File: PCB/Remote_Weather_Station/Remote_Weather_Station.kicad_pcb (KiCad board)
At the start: 4 copper layers, 0 parts

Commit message: Add files via upload
Laid out PDN
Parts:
- added C101: 1u, Capacitor_SMD:C_0805_2012Metric, F.Cu at (176.0, 92.3)
- added C102: 1u, Capacitor_SMD:C_0805_2012Metric, F.Cu at (176.0, 95.3)
- added C103: 100n, Capacitor_SMD:C_0805_2012Metric, F.Cu at (176.0, 98.3)
- added C104: 1u, Capacitor_SMD:C_0805_2012Metric, F.Cu at (176.0, 101.3)
- added C105: 1u, Capacitor_SMD:C_0805_2012Metric, F.Cu at (176.0, 104.4)
- added C106: 1u, Capacitor_SMD:C_0805_2012Metric, F.Cu at (176.0, 107.4)
- added C107: 1u, Capacitor_SMD:C_0805_2012Metric, F.Cu at (180.5, 92.3)
- added C108: 1u, Capacitor_SMD:C_0805_2012Metric, F.Cu at (180.5, 95.3)
- added C109: 1u, Capacitor_SMD:C_0805_2012Metric, F.Cu at (180.5, 98.3)
- added C110: 1u, Capacitor_SMD:C_0805_2012Metric, F.Cu at (180.5, 101.3)
- added C111: 1u, Capacitor_SMD:C_0805_2012Metric, F.Cu at (180.5, 104.4)
- added C112: 1u, Capacitor_SMD:C_0805_2012Metric, F.Cu at (180.5, 107.4)
- added C113: 1u, Capacitor_SMD:C_0805_2012Metric, F.Cu at (184.9, 92.3)
- added C114: 1u, Capacitor_SMD:C_0805_2012Metric, F.Cu at (184.9, 95.3)
- added C115: 1u, Capacitor_SMD:C_0805_2012Metric, F.Cu at (184.9, 98.3)
- added C116: 1u, Capacitor_SMD:C_0805_2012Metric, F.Cu at (184.9, 101.3)
- added C117: 1u, Capacitor_SMD:C_0805_2012Metric, F.Cu at (184.9, 104.4)
- added C201: 100n, Capacitor_SMD:C_0805_2012Metric, F.Cu at (47.4, 98.2)
- added C202: 10u, Capacitor_SMD:C_0805_2012Metric, F.Cu at (39.6, 102.5)
- added C203: 10u, Capacitor_SMD:C_0805_2012Metric, F.Cu at (39.6, 100.4)
- added C204: 47u, Capacitor_SMD:C_1206_3216Metric, F.Cu at (56.5, 99.6)
- added C205: 10u, Capacitor_SMD:C_0805_2012Metric, F.Cu at (60.5, 104.5)
- added C206: 22u, Capacitor_SMD:C_1206_3216Metric, F.Cu at (71.7, 101.1)
- added C207: 10u, Capacitor_SMD:C_0805_2012Metric, F.Cu at (60.6, 116.8)
- added C208: 22u, Capacitor_SMD:C_1206_3216Metric, F.Cu at (71.6, 113.9)
- added C209: 100n, Capacitor_SMD:C_0805_2012Metric, F.Cu at (47.5, 110.9)
- added C210: 10u, Capacitor_SMD:C_0805_2012Metric, F.Cu at (39.9, 113.1)
- added C211: 10u, Capacitor_SMD:C_0805_2012Metric, F.Cu at (39.9, 115.1)
- added C212: 47u, Capacitor_SMD:C_1206_3216Metric, F.Cu at (56.7, 112.3)
- added D101: RED_LED, LED_SMD:LED_0603_1608Metric, F.Cu at (188.9, 125.5)
- added H101: MountingHole, MountingHole:MountingHole_2.7mm_M2.5, F.Cu at (151.5, 56.6)
- added H102: MountingHole, MountingHole:MountingHole_2.7mm_M2.5, F.Cu at (151.5, 63.5)
- added H103: MountingHole, MountingHole:MountingHole_2.7mm_M2.5, F.Cu at (151.5, 70.5)
- added H104: MountingHole, MountingHole:MountingHole_2.7mm_M2.5, F.Cu at (151.5, 77.4)
- added J101: UART, Connector_PinHeader_2.54mm:PinHeader_1x06_P2.54mm_Vertical, F.Cu at (184.5, 111.2)
- added J102: Stemma_QT_Connector, Connector_JST:JST_SH_BM04B-SRSS-TB_1x04-1MP_P1.00mm_Vertical, F.Cu at (191.3, 121.1)
- added J103: wire_bus, Terminal_Blocks:WJ250B-3.5-12P-11-00A, F.Cu at (164.9, 164.5)
- added J105: power_in, Terminal_Blocks:DBT50G-7.62-4P-BK-P, F.Cu at (106.5, 101.5)
- added L201: 4.7u, Inductor_SMD:L_Vishay_IFSC-1515AH_4x4x1.8mm, F.Cu at (51.4, 99.5)
- added L202: 4.7u, Inductor_SMD:L_Vishay_IFSC-1515AH_4x4x1.8mm, F.Cu at (51.7, 112.2)
- added R101: 680, Resistor_SMD:R_0603_1608Metric_Pad0.98x0.95mm_HandSolder, F.Cu at (162.9, 92.1)
- added R102: 4.7k, Resistor_SMD:R_0603_1608Metric_Pad0.98x0.95mm_HandSolder, F.Cu at (162.9, 94.6)
- added R103: 20, Resistor_SMD:R_0603_1608Metric_Pad0.98x0.95mm_HandSolder, F.Cu at (162.9, 97.1)
- added R104: 330, Resistor_SMD:R_0603_1608Metric_Pad0.98x0.95mm_HandSolder, F.Cu at (162.9, 99.6)
- added R105: 4.7k, Resistor_SMD:R_0603_1608Metric_Pad0.98x0.95mm_HandSolder, F.Cu at (162.9, 102.1)
- added R106: 4.7k, Resistor_SMD:R_0603_1608Metric_Pad0.98x0.95mm_HandSolder, F.Cu at (162.9, 104.6)
- added R107: 20, Resistor_SMD:R_0603_1608Metric_Pad0.98x0.95mm_HandSolder, F.Cu at (162.9, 107.1)
- added R108: 330, Resistor_SMD:R_0603_1608Metric_Pad0.98x0.95mm_HandSolder, F.Cu at (162.9, 109.6)
- added R109: 4.7k, Resistor_SMD:R_0603_1608Metric_Pad0.98x0.95mm_HandSolder, F.Cu at (167.3, 92.1)
- added R110: 820, Resistor_SMD:R_0603_1608Metric_Pad0.98x0.95mm_HandSolder, F.Cu at (167.3, 94.6)
- added R111: 15k, Resistor_SMD:R_0603_1608Metric_Pad0.98x0.95mm_HandSolder, F.Cu at (167.3, 97.1)
- added R112: 15k, Resistor_SMD:R_0603_1608Metric_Pad0.98x0.95mm_HandSolder, F.Cu at (167.3, 99.6)
- added R113: 10k, Resistor_SMD:R_0603_1608Metric_Pad0.98x0.95mm_HandSolder, F.Cu at (167.3, 102.1)
- added R114: 1k, Resistor_SMD:R_0603_1608Metric_Pad0.98x0.95mm_HandSolder, F.Cu at (167.3, 104.6)
- added R115: 10k, Resistor_SMD:R_0603_1608Metric_Pad0.98x0.95mm_HandSolder, F.Cu at (167.3, 107.1)
- added R116: 1k, Resistor_SMD:R_0603_1608Metric_Pad0.98x0.95mm_HandSolder, F.Cu at (167.3, 109.6)
- added R117: 10k, Resistor_SMD:R_0603_1608Metric_Pad0.98x0.95mm_HandSolder, F.Cu at (171.6, 92.1)
- added R118: 4.7k, Resistor_SMD:R_0603_1608Metric_Pad0.98x0.95mm_HandSolder, F.Cu at (171.6, 94.6)
- added R119: 4.7k, Resistor_SMD:R_0603_1608Metric_Pad0.98x0.95mm_HandSolder, F.Cu at (171.6, 97.1)
- added R120: 4.7k, Resistor_SMD:R_0603_1608Metric_Pad0.98x0.95mm_HandSolder, F.Cu at (171.6, 99.6)
- added R121: 1k, Resistor_SMD:R_0603_1608Metric_Pad0.98x0.95mm_HandSolder, F.Cu at (171.6, 102.1)
- added R201: 49.9k, Resistor_SMD:R_0603_1608Metric_Pad0.98x0.95mm_HandSolder, F.Cu at (54.5, 98.9)
- added R202: 10k, Resistor_SMD:R_0603_1608Metric_Pad0.98x0.95mm_HandSolder, F.Cu at (54.5, 102.2)
- added R203: 0, Resistor_SMD:R_0603_1608Metric_Pad0.98x0.95mm_HandSolder, F.Cu at (71.7, 105.1)
- added R204: 0, Resistor_SMD:R_0603_1608Metric_Pad0.98x0.95mm_HandSolder, F.Cu at (71.6, 117.9)
- added R205: 68k, Resistor_SMD:R_0603_1608Metric_Pad0.98x0.95mm_HandSolder, F.Cu at (54.8, 111.6)
- added R206: 10k, Resistor_SMD:R_0603_1608Metric_Pad0.98x0.95mm_HandSolder, F.Cu at (54.8, 118.2)
- added R207: 3.6k, Resistor_SMD:R_0603_1608Metric_Pad0.98x0.95mm_HandSolder, F.Cu at (54.8, 114.9)
- added SW101: SW_Push, Button_Switch_SMD:SW_SPST_TS-1088-xR020, F.Cu at (190.4, 111.2)
- added SW102: SW_Push, Button_Switch_SMD:SW_SPST_TS-1088-xR020, F.Cu at (190.4, 115.7)
- added U101: ESP32-WROOM-32D, RF_Module:ESP32-WROOM-32D, F.Cu at (131.6, 76.1)
- added U102: AD8227, Package_SO:SOIC-8_3.9x4.9mm_P1.27mm, F.Cu at (178.0, 112.2)
- added U103: AD8227, Package_SO:SOIC-8_3.9x4.9mm_P1.27mm, F.Cu at (178.0, 118.8)
- added U104: AD8227, Package_SO:SOIC-8_3.9x4.9mm_P1.27mm, F.Cu at (178.0, 125.4)
- added U105: SIM7600X, Modem_Footprint:SIM7600X, F.Cu at (137.3, 111.0)
- added U201: TPS561208DDCR, Package_TO_SOT_SMD:SOT-23-6, F.Cu at (43.5, 99.0)
- added U202: AMS1117-3.3, Package_TO_SOT_SMD:SOT-223-3_TabPin2, F.Cu at (66.0, 101.0)
- added U203: AMS1117-5.0, Package_TO_SOT_SMD:SOT-223-3_TabPin2, F.Cu at (66.0, 113.6)
- added U204: TPS561201DDCR, Package_TO_SOT_SMD:SOT-23-6, F.Cu at (43.7, 111.4)

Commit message: Add files via upload
PDN PCB v.1
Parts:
- moved C208 5.88 mm to (77.4, 114.8)
- moved R204 5.88 mm to (77.4, 118.9)
- moved U202 5.86 mm to (71.8, 100.7)
- moved U203 5.81 mm to (71.8, 113.3)
- moved R203 5.81 mm to (77.4, 106.2)
- moved C206 5.81 mm to (77.4, 102.2)
- moved C205 5.12 mm to (64.5, 101.2)
- moved C212 5.11 mm to (61.8, 112.0)
- moved C204 5.10 mm to (61.6, 99.5)
- moved C207 5.00 mm to (64.5, 113.7)
- moved R201 4.30 mm to (58.8, 98.9)
- moved R202 4.30 mm to (58.8, 102.2)
- moved R205 4.00 mm to (58.8, 111.5)
- moved R206 4.00 mm to (58.8, 118.1)
- moved R207 4.00 mm to (58.8, 114.8)
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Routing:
- net +12V: track 0.00 -> 21.2 mm
- net /PDN/6.3V_OUT: track 0.00 -> 18.7 mm
- net /PDN/4.6V_OUT: track 0.00 -> 18.6 mm
- net Net-(U204-VFB): track 0.00 -> 17.2 mm, vias 0 -> 2
- net Net-(U201-VFB): track 0.00 -> 15.9 mm, vias 0 -> 2
- net Net-(U201-SW): track 0.00 -> 11.2 mm, vias 0 -> 2
- net Net-(U204-SW): track 0.00 -> 11.0 mm, vias 0 -> 2
- net +5V: track 0.00 -> 8.70 mm, vias 0 -> 2
- net +3.3V: track 0.00 -> 8.70 mm, vias 0 -> 2
- net Net-(U201-VBST): track 0.00 -> 2.80 mm
- net Net-(U204-VBST): track 0.00 -> 2.69 mm
- net Net-(C208-Pad2): track 0.00 -> 1.65 mm
- net Net-(C206-Pad2): track 0.00 -> 1.65 mm
- net Net-(R205-Pad2): track 0.00 -> 1.50 mm
- net GND: vias 0 -> 16

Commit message: Add files via upload
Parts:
- added C106: 1u, Capacitor_SMD:C_0805_2012Metric, F.Cu at (89.7, 139.2)
- added C107: 1u, Capacitor_SMD:C_0805_2012Metric, F.Cu at (89.7, 142.2)
- added C120: 1u, Capacitor_SMD:C_0805_2012Metric, F.Cu at (89.7, 145.2)
- added C121: 1u, Capacitor_SMD:C_0805_2012Metric, F.Cu at (89.7, 148.2)
- added R102: 11k, Resistor_SMD:R_0603_1608Metric_Pad0.98x0.95mm_HandSolder, F.Cu at (94.1, 139.0)
- added R103: 11k, Resistor_SMD:R_0603_1608Metric_Pad0.98x0.95mm_HandSolder, F.Cu at (94.1, 141.5)
- added R124: 11k, Resistor_SMD:R_0603_1608Metric_Pad0.98x0.95mm_HandSolder, F.Cu at (94.1, 144.0)
- added R125: 11k, Resistor_SMD:R_0603_1608Metric_Pad0.98x0.95mm_HandSolder, F.Cu at (94.1, 146.5)
- renumbered C103 to C102, C104 to C103, C102 to C104, C106 to C108, C107 to C109, C108 to C110, C109 to C111, C110 to C112, C111 to C113, C112 to C114, C113 to C115, C117 to C116, C114 to C117, C115 to C118, C116 to C119, R102 to R104, R103 to R105, R104 to R106, R105 to R107, R106 to R108, R107 to R109, R108 to R110, R109 to R111, R110 to R112, R111 to R113, R112 to R114, R113 to R115, R114 to R116, R115 to R117, R116 to R118, R117 to R119, R121 to R120, R118 to R121, R119 to R122, R120 to R123, R207 to R206, R206 to R207, U105 to U102, U102 to U103, U103 to U104, U104 to U105
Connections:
- J102 pad MP: (no net) -> GND
- J103 pad 10: Green_Wire -> Green_Wire_in
- J103 pad 11: White_Wire -> White_Wire_in
- J103 pad 2: North_South_Ref -> /N_red_wire
- J103 pad 4: East_West_Ref -> /E_red_wire
- J103 pad 5: North_South_Ref -> /N_red_wire
- J103 pad 7: East_West_Ref -> /E_red_wire
- U103 pad 1: Green_Wire -> White_Wire
- U103 pad 4: White_Wire -> Green_Wire

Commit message: Add files via upload
PCB Progress, Layout coming along
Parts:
- R102, R103: value 11k -> 10k
- R112: renamed from R124; value 11k -> 10k
- R113: renamed from R125; value 11k -> 10k
- moved C101 133.1 mm to (43.0, 93.2)
- moved C104 133.1 mm to (43.0, 96.2)
- moved C105 133.1 mm to (43.0, 105.3)
- moved C109 133.1 mm to (47.4, 93.2)
- moved C110 133.1 mm to (47.4, 96.2)
- moved C111 133.1 mm to (47.4, 99.2)
- moved C115 133.1 mm to (47.4, 105.3)
- moved C116 133.1 mm to (47.4, 108.3)
- moved C117 133.1 mm to (51.9, 93.2)
- moved C118 133.1 mm to (51.9, 105.3)
- moved C119 133.1 mm to (51.9, 96.2)
- moved C120 133.1 mm to (51.9, 99.2)
- moved C121 133.1 mm to (51.9, 102.2)
- moved D101 133.1 mm to (55.8, 126.4)
- moved R101 133.1 mm to (29.9, 93.0)
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- renumbered C120 to C113, C121 to C114, C113 to C115, C114 to C116, C115 to C117, C116 to C118, C117 to C119, C118 to C120, C119 to C121, R112 to R114, R113 to R115, R114 to R116, R115 to R117, R116 to R118, R117 to R119, R118 to R120, R119 to R121, R120 to R122, R121 to R123, R122 to R124, R123 to R125
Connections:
- U101 pad 11: unconnected-(U101-IO26-Pad11) -> modem_tx
- U101 pad 12: unconnected-(U101-IO27-Pad12) -> modem_rx
- U102 pad 21: unconnected-(U102-RXD-Pad21) -> modem_rx
- U102 pad 22: unconnected-(U102-TXD-Pad22) -> modem_tx
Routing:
- net modem_rx: track 0.00 -> 42.9 mm
- net Flash: track 0.00 -> 42.3 mm, vias 0 -> 1
- net modem_tx: track 0.00 -> 39.4 mm
- net TX: track 0.00 -> 36.9 mm, vias 0 -> 1
- net RX: track 0.00 -> 33.7 mm, vias 0 -> 1
- net Reset: track 0.00 -> 21.1 mm
- net +3.3V: track 8.70 -> 16.0 mm
- net GND: vias 16 -> 24
- added copper zone on In2.Cu, net +12V

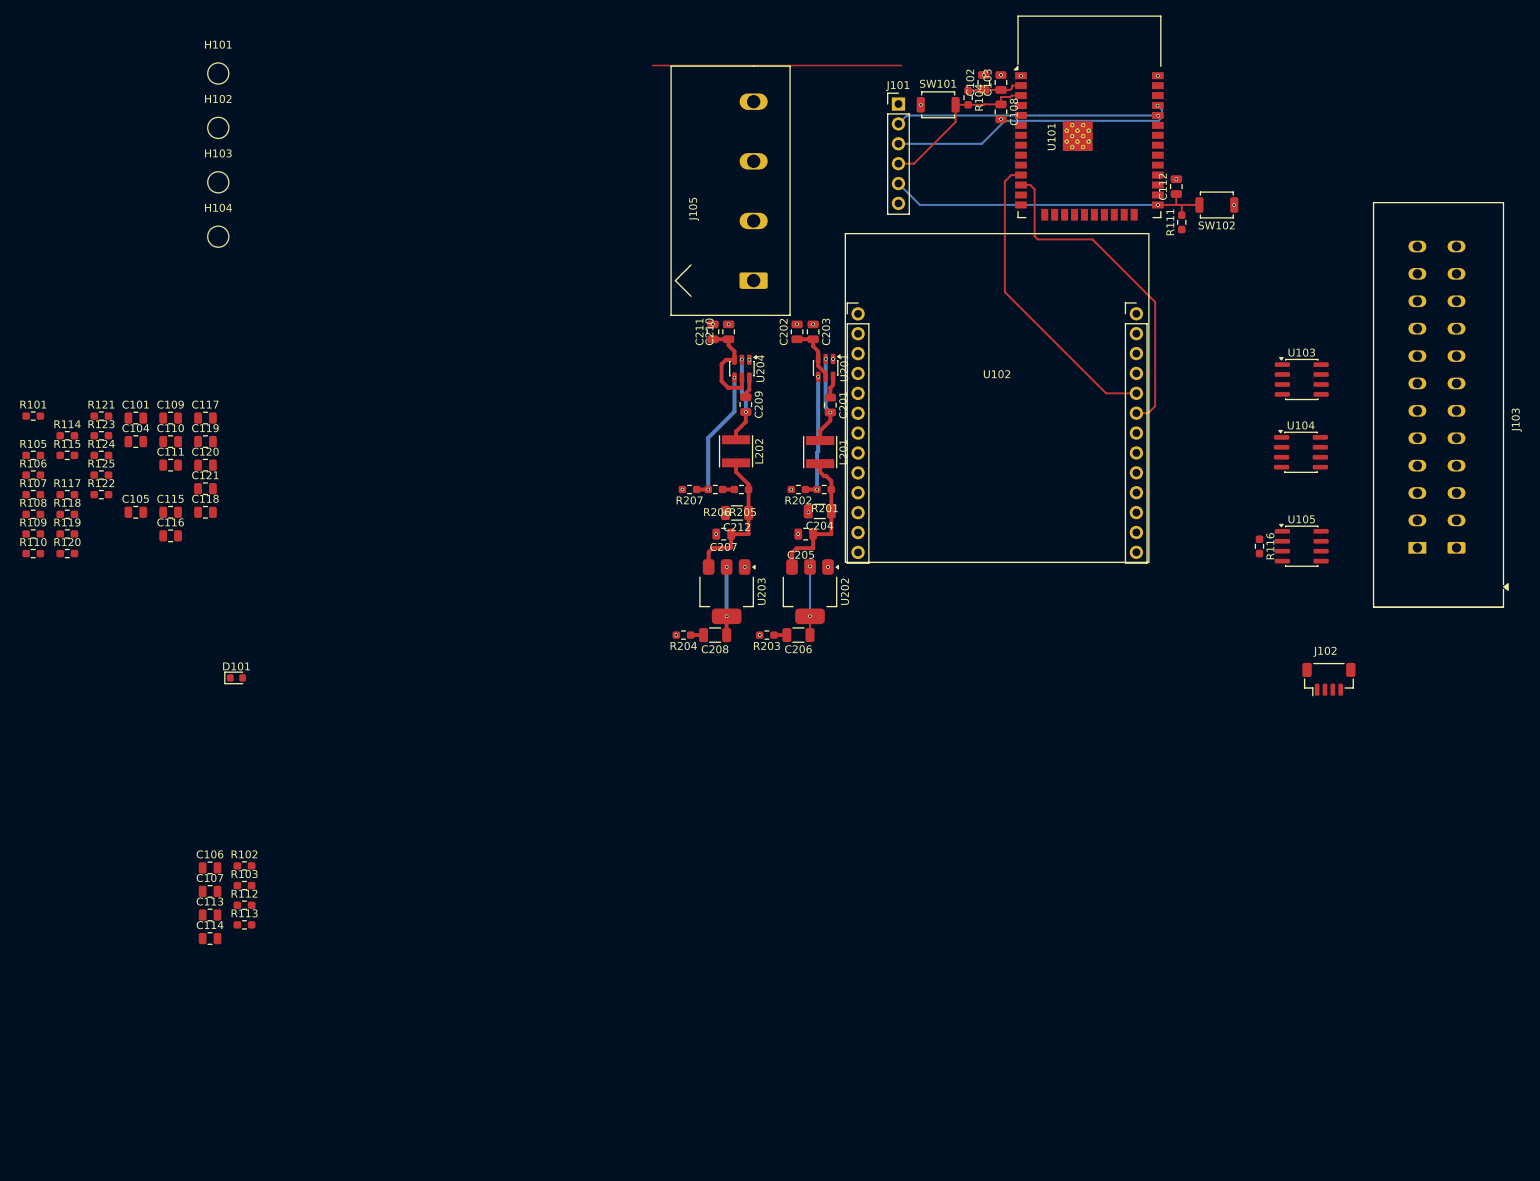
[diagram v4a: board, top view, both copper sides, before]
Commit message: Vias
Vias should be added and tied to pads
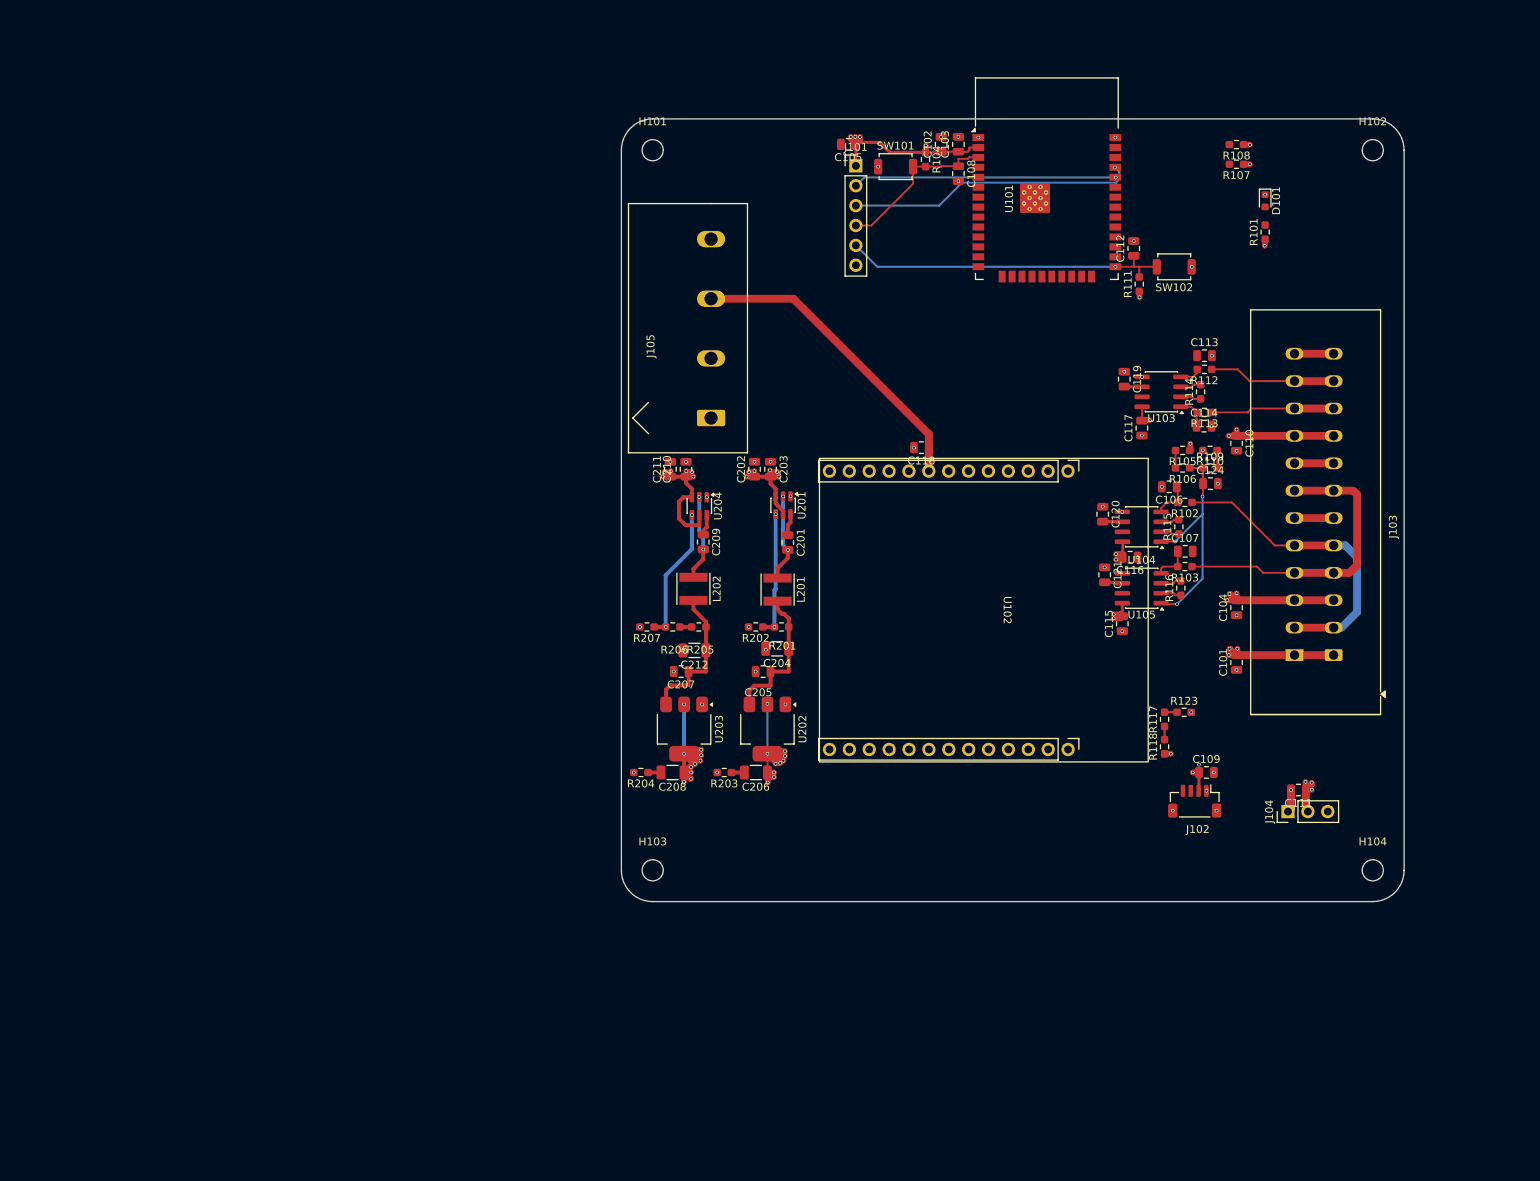
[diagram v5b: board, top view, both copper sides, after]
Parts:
- removed R119, R121: 10k, Resistor_SMD:R_0603_1608Metric_Pad0.98x0.95mm_HandSolder
- removed R120, R122: 1k, Resistor_SMD:R_0603_1608Metric_Pad0.98x0.95mm_HandSolder
- removed R124, R125: 4.7k, Resistor_SMD:R_0603_1608Metric_Pad0.98x0.95mm_HandSolder
- added C124: 1u, Capacitor_SMD:C_0805_2012Metric, F.Cu at (180.3, 101.6)
- added J104: Servo_Connector, Connector_PinHeader_2.54mm:PinHeader_1x03_P2.54mm_Vertical, F.Cu at (190.2, 143.5)
- moved H104 168.3 mm to (201.0, 151.0)
- moved R108 160.8 mm to (183.6, 58.3), turned to 180 degrees
- moved R107 159.4 mm to (183.6, 60.8), turned to 180 degrees
- moved R101 159.1 mm to (187.2, 69.5), turned to 90 degrees
- moved R110 150.9 mm to (180.2, 97.3), turned to 180 degrees
- moved R109 150.6 mm to (180.2, 99.6)
- moved C111 149.9 mm to (191.5, 140.8), turned to 180 degrees
- moved H102 147.5 mm to (201.0, 59.0)
- moved R106 146.9 mm to (176.7, 99.6), turned to 180 degrees
- moved R105 146.9 mm to (176.7, 97.3), turned to 180 degrees
- moved C113 145.8 mm to (179.5, 85.2)
- moved R114 144.9 mm to (179.0, 89.9), turned to 90 degrees
- moved D101 144.9 mm to (187.2, 65.5), turned to -90 degrees
- moved C101 144.1 mm to (183.6, 124.5), turned to 90 degrees
- moved R118 143.3 mm to (174.4, 135.2), turned to 90 degrees
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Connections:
- C105 pad 1: +5V -> +3.3V
- C119 pad 2: Net-(U103-Ref) -> /V_ref_amp
- C120 pad 2: Net-(U104-Ref) -> /V_ref_amp
- C121 pad 2: Net-(U105-Ref) -> /V_ref_amp
- J101 pad 1: +5V -> +3.3V
- J103 pad 10: Green_Wire_in -> /rain_white
- J103 pad 11: White_Wire_in -> /rain_green
- R112 pad 1: Green_Wire_in -> /rain_green
- R113 pad 1: White_Wire_in -> /rain_white
- R117 pad 2: Net-(U103-Ref) -> /V_ref_amp
- R123 pad 1: Net-(U103-Ref) -> /V_ref_amp
- U101 pad 11: modem_tx -> modem_rx
- U101 pad 12: modem_rx -> modem_tx
- U103 pad 6: Net-(U103-Ref) -> /V_ref_amp
- U104 pad 6: Net-(U104-Ref) -> /V_ref_amp
- U105 pad 6: Net-(U105-Ref) -> /V_ref_amp
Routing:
- net +3.3V: track 16.0 -> 96.4 mm, vias 2 -> 27
- net modem_rx: track 42.9 -> 0.00 mm
- net /N_red_wire: track 0.00 -> 39.8 mm
- net +5V_panel: track 0.00 -> 39.7 mm
- net modem_tx: track 39.4 -> 0.00 mm
- net /E_red_wire: track 0.00 -> 39.0 mm
- net +5V: track 8.70 -> 43.1 mm, vias 2 -> 21
- net Base_Ref: track 0.00 -> 29.3 mm, vias 0 -> 3
- net GND: track 0.00 -> 18.0 mm, vias 24 -> 48
- net /rain_green: track 0.00 -> 16.2 mm
- net /rain_white: track 0.00 -> 15.8 mm
- net +12V: track 20.7 -> 31.8 mm, vias 0 -> 12
- net /V_ref_amp: track 0.00 -> 8.70 mm
- net North_South_Ref: track 0.00 -> 4.97 mm
- net East_West_Ref: track 0.00 -> 4.80 mm
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- added copper zone on In2.Cu, net +3.3V
- added copper zone on In2.Cu, net +5V
- added copper zone on In1.Cu, net GND
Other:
- board outline added: 100 x 100 mm
